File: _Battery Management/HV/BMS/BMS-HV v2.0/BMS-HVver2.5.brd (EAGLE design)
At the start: 152.4 x 124.8 mm, 452 parts, among them J3 M2S02B-PASK-2(LF)(SN), J4 M2S02B-PASK-2(LF)(SN), Q1 BSS308PE, Q10 BSS308PE, Q11 BSS308PE, Q12 BSS308PE, Q13 BSS308PE, Q14 BSS308PE, Q15 BSS308PE, Q16 BSS308PE, Q17 BSS308PE, Q18 BSS308PE, Q19 BSS308PE, Q2 BSS308PE, Q20 BSS308PE, Q21 BSS308PE, Q22 BSS308PE, Q23 BSS308PE, Q24 BSS308PE, Q25 BSS308PE, Q26 BSS308PE, Q27 BSS308PE, Q28 BSS308PE, Q29 BSS308PE, Q3 BSS308PE, Q30 BSS308PE, Q31 BSS308PE, Q32 BSS308PE, Q33 BSS308PE, Q34 BSS308PE, Q35 BSS308PE, Q36 BSS308PE, Q37 BSS308PE, Q38 BSS308PE, Q39 BSS308PE, Q4 BSS308PE, Q5 BSS308PE, Q6 BSS308PE, Q7 BSS308PE, Q8 BSS308PE, Q9 BSS308PE, U1 LTC6804-2, U2 LTC6804-2, U3 LTC6804-2

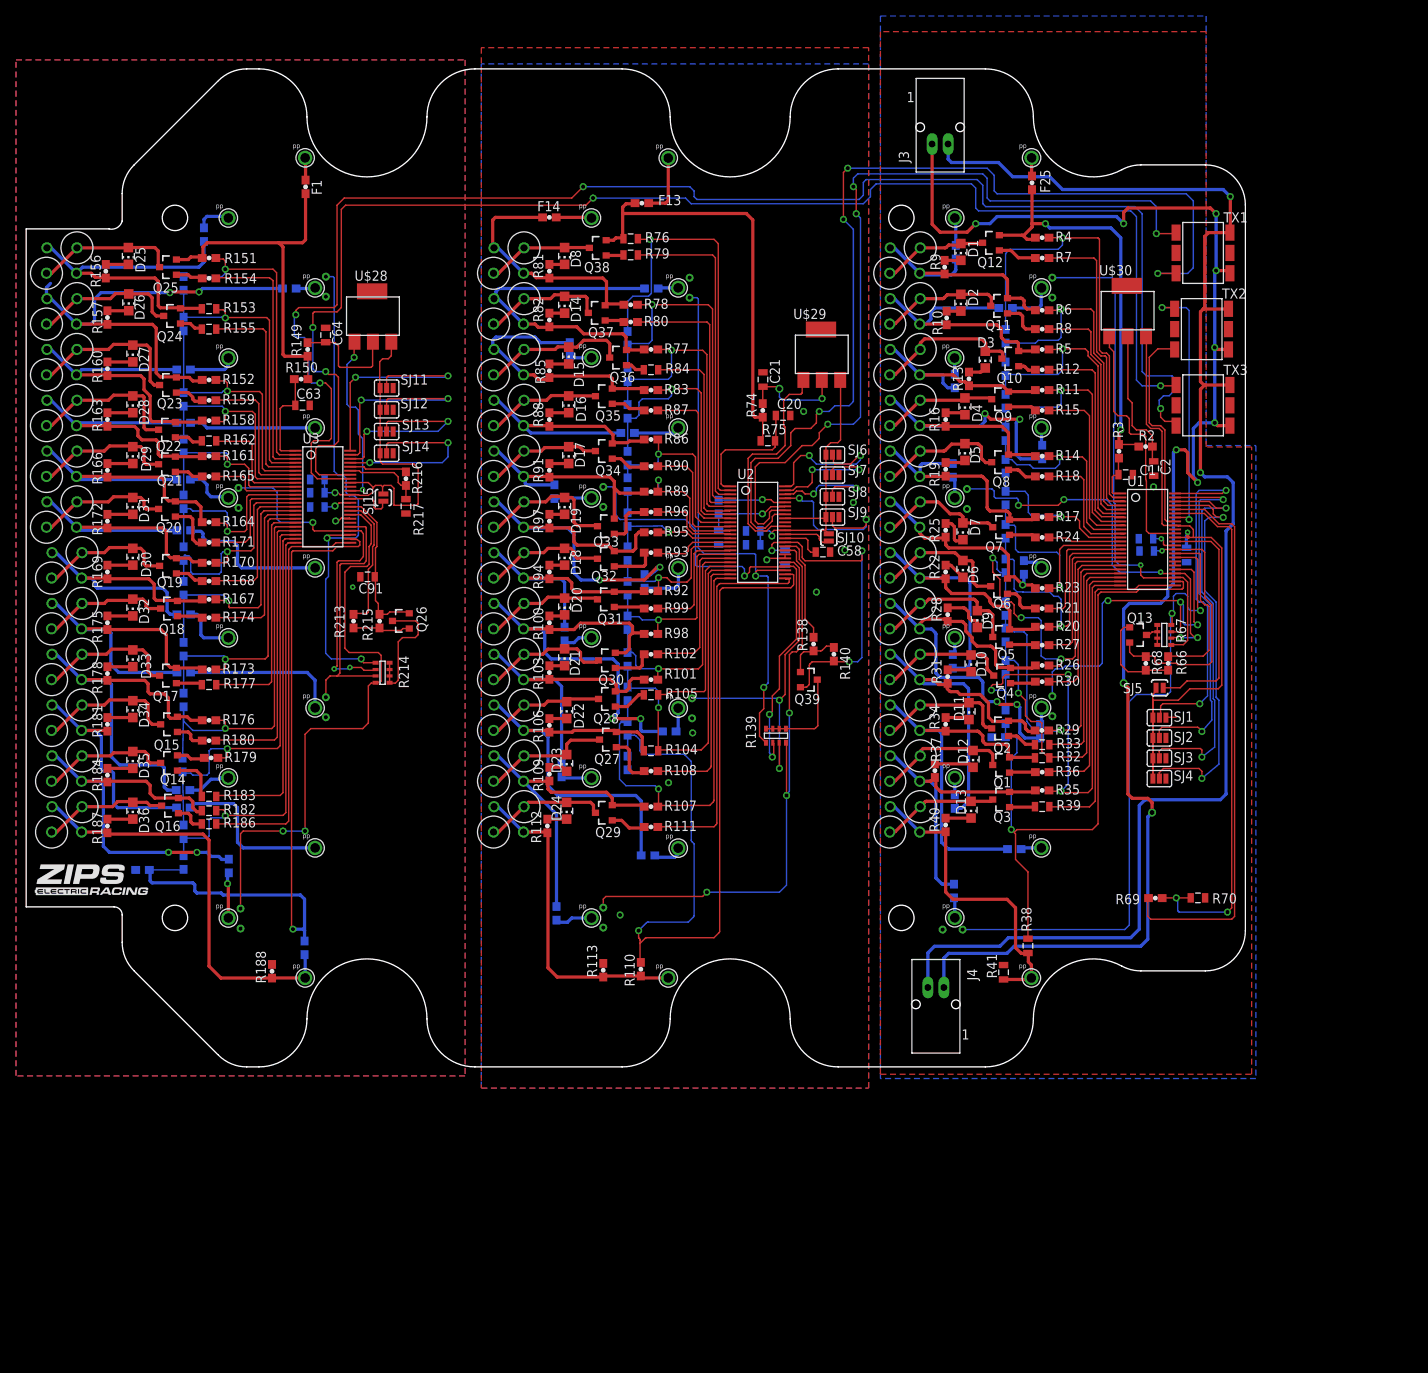
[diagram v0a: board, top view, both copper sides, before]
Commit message: 
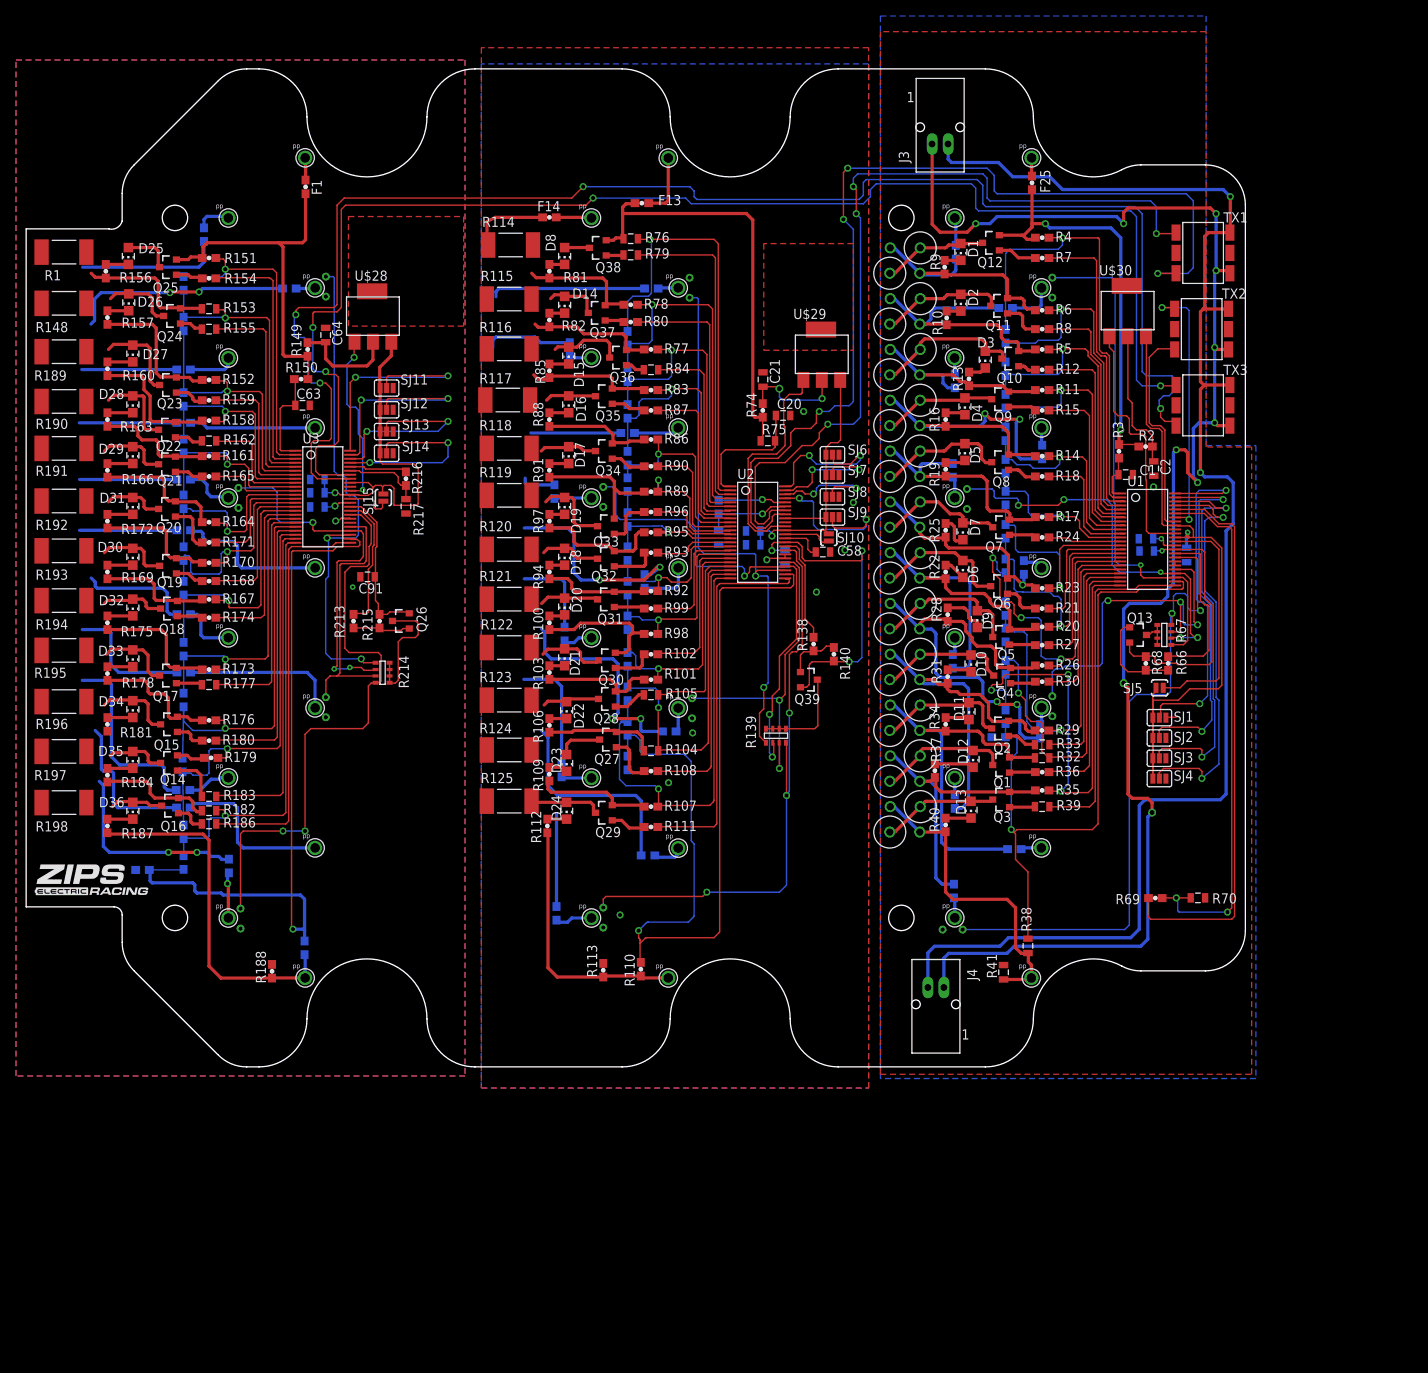
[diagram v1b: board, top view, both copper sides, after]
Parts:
- removed R126, R127, R128, R129, R130, R131, R132, R133, R134, R135, R136, R137, R199, R200, R201, R202, R203, R204, R205, R206, R207, R208, R209, R210, R211, R212: 16, FSAE Electric:RR02J16RTB
- added R1, R148: (no value), adafruit:R2512
- R114, R115, R116, R117, R118, R119, R120, R121, R122, R123, R124, R125, R189, R190, R191, R192, R193, R194, R195, R196, R197, R198: value 16 -> (none); device FSAE Electric:RR02J16RTB -> adafruit:R2512
- moved R114 73.4 mm to (-15.6, 40.4), turned to 0 degrees
- moved R115 63.5 mm to (-15.8, 33.6)
- moved R189 60.1 mm to (-71.5, 27.0), turned to 0 degrees
- moved R116 54.1 mm to (-15.8, 27.4), turned to 0 degrees
- moved R190 50.7 mm to (-71.5, 20.8)
- moved R117 44.5 mm to (-16.0, 21.0)
- moved R191 41.6 mm to (-71.5, 14.9), turned to 0 degrees
- moved R118 35.3 mm to (-15.8, 14.9), turned to 0 degrees
- moved R192 31.9 mm to (-71.5, 8.36)
- moved R125 31.1 mm to (-15.8, -29.2)
- moved R119 26.3 mm to (-15.8, 9.07)
- moved R198 25.0 mm to (-71.5, -29.3)
- moved R193 22.5 mm to (-71.5, 2.13), turned to 0 degrees
- moved R124 21.6 mm to (-15.8, -22.8), turned to 0 degrees
- moved R120 16.4 mm to (-15.8, 2.31), turned to 0 degrees
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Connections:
- net N$101: now also R198.2; no longer R189.P$2, R190.P$2
- net N$103: now also R114.2; no longer R136.P$2, R137.P$2
- net N$105: now also R198.1; no longer R189.P$1, R190.P$1
- net N$106: now also R197.1; no longer R191.P$1, R192.P$1
- net N$108: now also R114.1; no longer R136.P$1, R137.P$1
- net N$111: now also R115.2; no longer R134.P$2, R135.P$2
- net N$113: now also R115.1; no longer R134.P$1, R135.P$1
- net N$116: now also R116.2; no longer R132.P$2, R133.P$2
- net N$118: now also R116.1; no longer R132.P$1, R133.P$1
- net N$122: now also R117.2; no longer R130.P$2, R131.P$2
- net N$124: now also R117.1; no longer R130.P$1, R131.P$1
- net N$127: now also R118.2; no longer R128.P$2, R129.P$2
- net N$131: now also R120.2; no longer R124.P$2, R125.P$2
- net N$134: now also R118.1; no longer R128.P$1, R129.P$1
- net N$137: now also R119.2; no longer R126.P$2, R127.P$2
- net N$139: now also R119.1; no longer R126.P$1, R127.P$1
- net N$142: now also R120.1; no longer R124.P$1, R125.P$1
- net N$145: now also R121.2; no longer R122.P$2, R123.P$2
- net N$147: now also R121.1; no longer R122.P$1, R123.P$1
- net N$150: now also R122.2; no longer R120.P$2, R121.P$2
- net N$152: now also R122.1; no longer R120.P$1, R121.P$1
- net N$155: now also R123.2; no longer R118.P$2, R119.P$2
- net N$159: now also R123.1; no longer R118.P$1, R119.P$1
- net N$162: now also R124.2; no longer R116.P$2, R117.P$2
- net N$175: now also R125.2; no longer R114.P$2, R115.P$2
- net N$176: now also R125.1; no longer R114.P$1, R115.P$1
- net N$177: now also R124.1; no longer R116.P$1, R117.P$1
- net N$56: now also R1.2; no longer R211.P$2, R212.P$2
- net N$58: now also R1.1; no longer R211.P$1, R212.P$1
- net N$60: now also R148.2; no longer R209.P$2, R210.P$2
- net N$62: now also R148.1; no longer R209.P$1, R210.P$1
- net N$64: now also R189.2; no longer R207.P$2, R208.P$2
- net N$66: now also R189.1; no longer R207.P$1, R208.P$1
- net N$68: now also R190.2; no longer R205.P$2, R206.P$2
- net N$70: now also R190.1; no longer R205.P$1, R206.P$1
- net N$72: now also R191.2; no longer R203.P$2, R204.P$2
- net N$75: now also R193.2; no longer R199.P$2, R200.P$2
- net N$77: now also R191.1; no longer R203.P$1, R204.P$1
- net N$79: now also R192.2; no longer R201.P$2, R202.P$2
- net N$81: now also R192.1; no longer R201.P$1, R202.P$1
- net N$82: now also R193.1; no longer R199.P$1, R200.P$1
- net N$84: now also R194.2; no longer R197.P$2, R198.P$2
- net N$86: now also R194.1; no longer R197.P$1, R198.P$1
- net N$88: now also R195.2; no longer R195.P$2, R196.P$2
- net N$90: now also R195.1; no longer R195.P$1, R196.P$1
- net N$92: now also R196.2; no longer R193.P$2, R194.P$2
- net N$94: now also R196.1; no longer R193.P$1, R194.P$1
- net N$96: now also R197.2; no longer R191.P$2, R192.P$2
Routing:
- net N$177: track 40.2 -> 26.1 mm
- net N$62: track 58.3 -> 45.5 mm
- net N$56: track 17.6 -> 6.06 mm
- net N$147: track 55.7 -> 45.3 mm
- net N$106: track 49.7 -> 39.4 mm
- net N$162: track 16.2 -> 5.86 mm
- net N$159: track 50.9 -> 40.6 mm
- net N$103: track 13.3 -> 3.15 mm
- net N$94: track 32.4 -> 22.5 mm
- net N$66: track 38.6 -> 28.9 mm
- net N$124: track 34.4 -> 25.0 mm
- net N$82: track 37.9 -> 28.5 mm
- net N$81: track 36.9 -> 27.6 mm
- net N$77: track 38.0 -> 28.7 mm
- net N$60: track 18.4 -> 9.11 mm
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- added copper zone on layer 1, net N$51
- added copper zone on layer 1, net N$54

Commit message: 
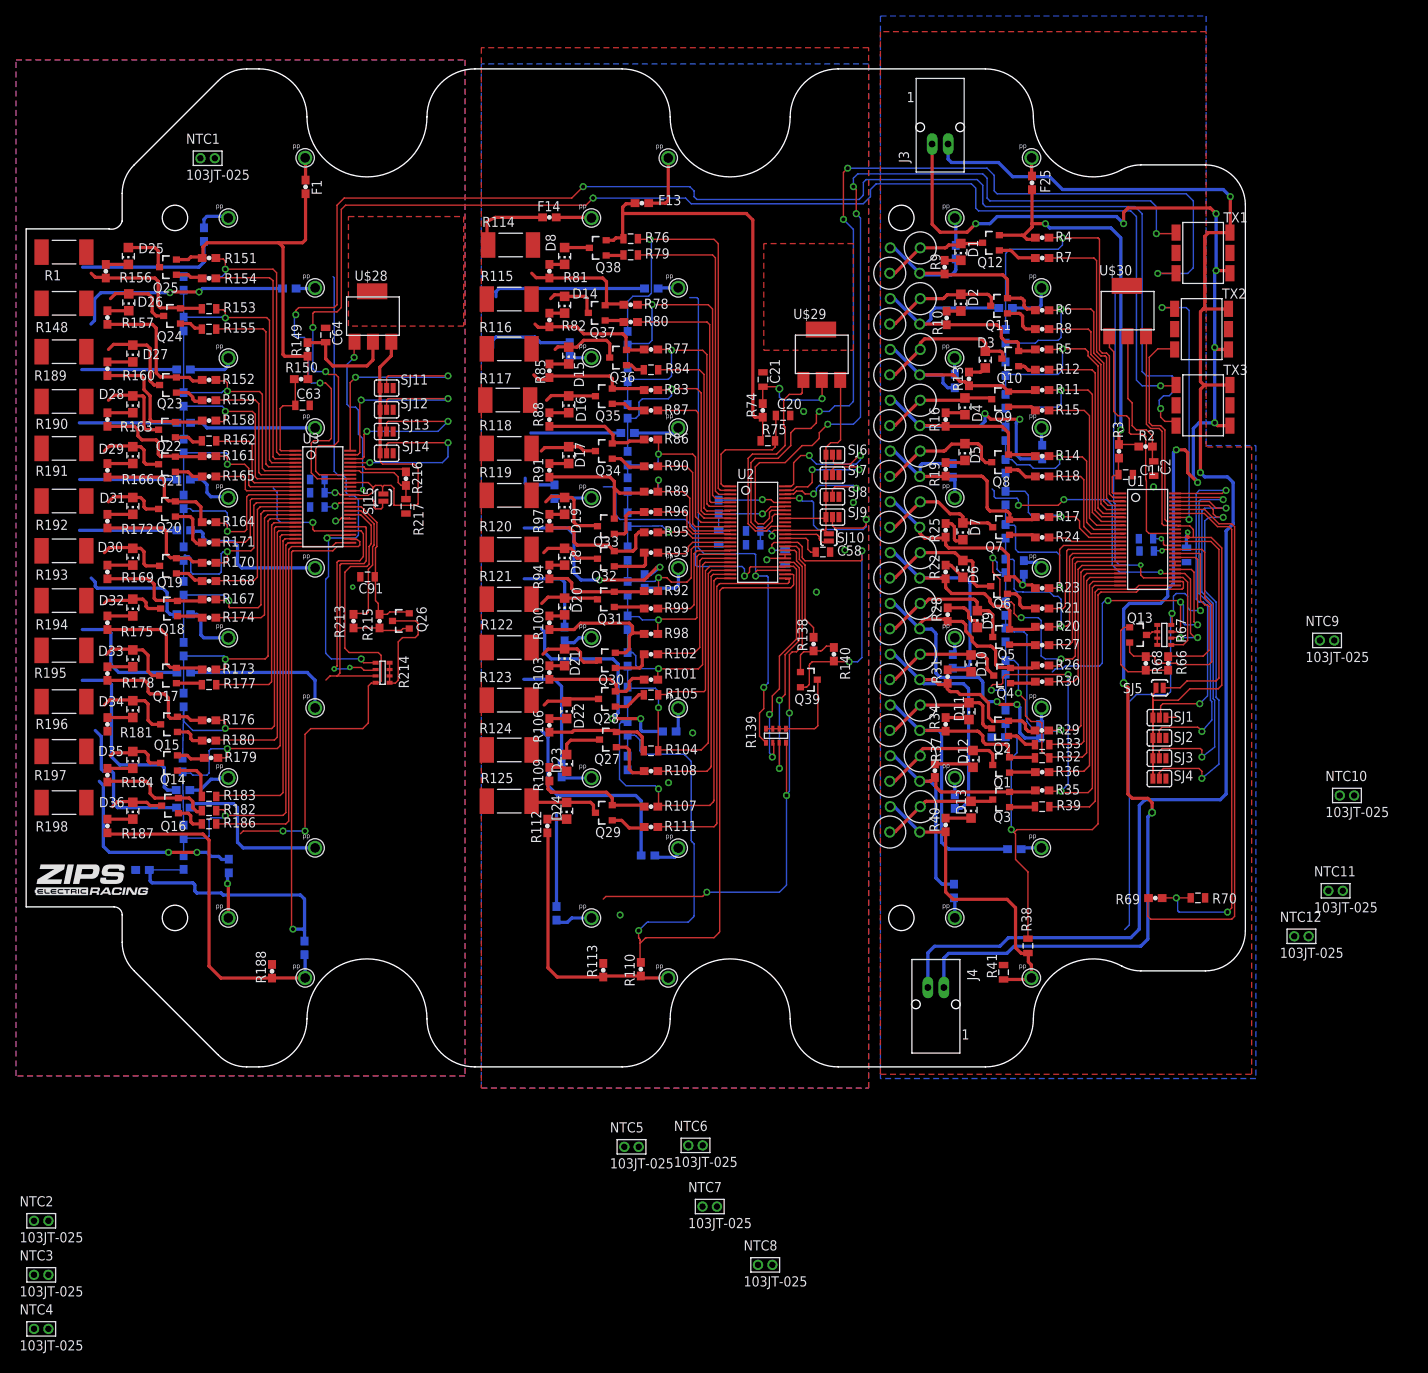
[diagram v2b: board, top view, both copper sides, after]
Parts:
- removed R143, R144, R145, R146, R147, R218, R219, R220, R221, R71, R72, R73: 10K-NTC, FSAE Electric:NTC-NXRT15XH103FA5B
- added NTC1, NTC10, NTC11, NTC12, NTC2, NTC3, NTC4, NTC5, NTC6, NTC7, NTC8, NTC9: 103JT-025, FSAE Electric:103JT-025
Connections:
- net GND: now also NTC1.1, NTC2.1, NTC3.1, NTC4.1; no longer R218.P$1, R219.P$1, R220.P$1, R221.P$1
- net GNDA: now also NTC5.1, NTC6.1, NTC7.1, NTC8.1; no longer R143.P$1, R144.P$1, R145.P$1, R146.P$1
- net GNDI: now also NTC10.1, NTC11.1, NTC12.1, NTC9.1; no longer R147.P$1, R71.P$1, R72.P$1, R73.P$1
- net GPIO1: now also NTC5.2; no longer R143.P$2
- net GPIO11: now also NTC2.2; no longer R219.P$2
- net GPIO12: now also NTC1.2; no longer R218.P$2
- net GPIO13: now also NTC4.2; no longer R221.P$2
- net GPIO14: now also NTC3.2; no longer R220.P$2
- net GPIO2: now also NTC6.2; no longer R144.P$2
- net GPIO3: now also NTC7.2; no longer R145.P$2
- net GPIO4: now also NTC8.2; no longer R146.P$2
- net GPIO6: now also NTC10.2; no longer R72.P$2
- net GPIO7: now also NTC9.2; no longer R71.P$2
- net GPIO8: now also NTC12.2; no longer R147.P$2
- net GPIO9: now also NTC11.2; no longer R73.P$2
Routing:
- net GPIO8: track 82.9 -> 62.7 mm
- net GPIO3: track 42.4 -> 31.7 mm
- net GPIO13: track 73.8 -> 64.5 mm
- net GPIO7: track 63.7 -> 56.2 mm
- net GPIO11: track 45.9 -> 41.6 mm
- net GPIO6: track 49.6 -> 46.4 mm
- net GPIO9: track 46.0 -> 42.9 mm
- net GPIO14: track 32.3 -> 30.2 mm
- net GPIO4: track 75.8 -> 74.8 mm
- net GPIO12: track 64.0 -> 63.0 mm
